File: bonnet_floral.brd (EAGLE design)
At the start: 65 x 30 mm, 10 parts, among them IC1 RASPBERRY_PI_ZERO_W_(V1.3)-WO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

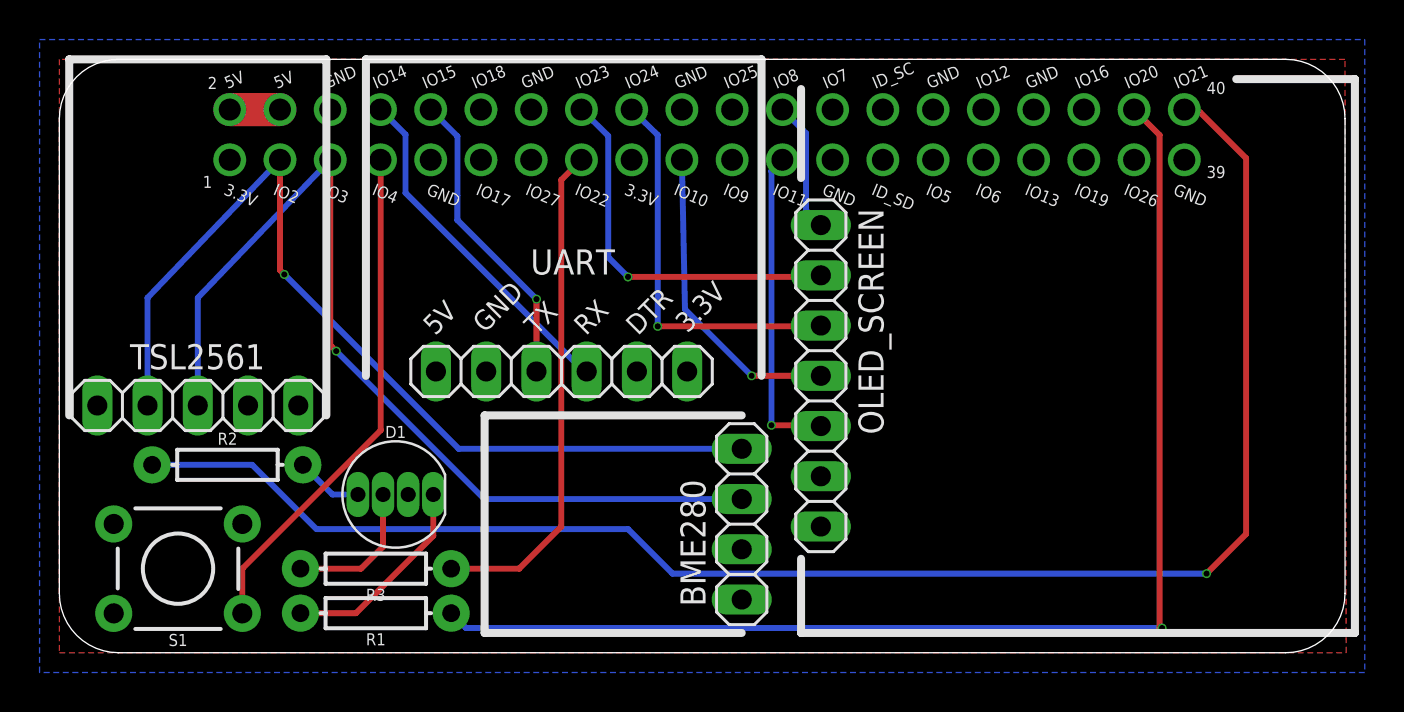
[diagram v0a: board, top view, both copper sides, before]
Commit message: Moving the BME280 down a little
The BME280 was right up against the lower side of the CP2102, so
I'm moving it down 1mm (and re-routing the signals as needed) to
give it a little bit of space.
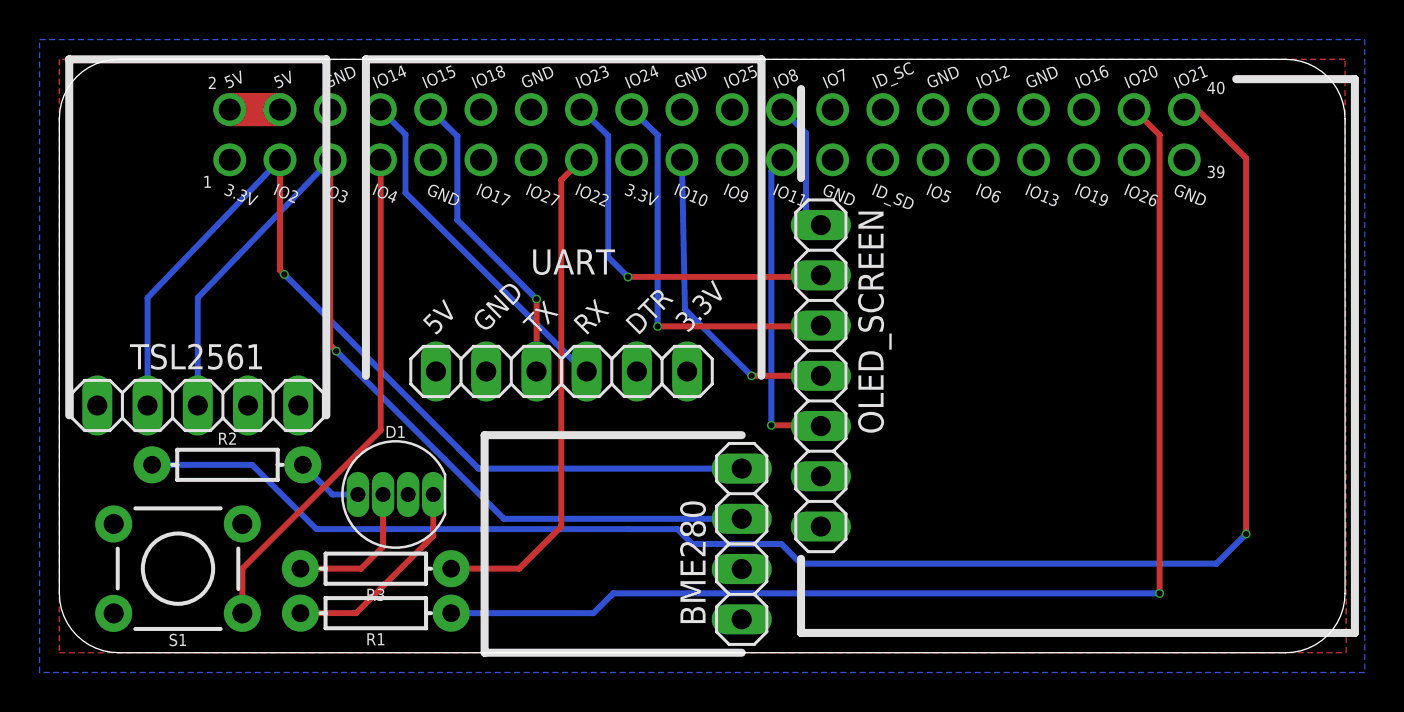
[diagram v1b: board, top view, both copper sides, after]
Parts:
- moved BME280 1.00 mm to (34.5, 5.50)
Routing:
- net RGB_R: track 63.1 -> 61.2 mm
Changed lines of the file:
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@@
 <setting verticaltext="up"/>
 </settings>
-<grid distance="1" unitdist="mm" unit="mm" style="lines" multiple="1" display="no" altdistance="0.125" altunitdist="mm" altunit="mm"/>
+<grid distance="1" unitdist="mm" unit="mm" style="lines" multiple="1" display="no" altdistance="0.5" altunitdist="mm" altunit="mm"/>
 <layers>
 <layer number="1" name="Top" color="4" fill="1" visible="yes" active="yes"/>
@@
 <wire x1="15.5" y1="30" x2="15.5" y2="14" width="0.4064" layer="21"/>
 <wire x1="35.5" y1="30" x2="15.5" y2="30" width="0.4064" layer="21"/>
-<wire x1="34.5" y1="1" x2="21.5" y2="1" width="0.4064" layer="21"/>
-<wire x1="21.5" y1="1" x2="21.5" y2="12" width="0.4064" layer="21"/>
-<wire x1="34.5" y1="12" x2="21.5" y2="12" width="0.4064" layer="21"/>
+<wire x1="34.5" y1="0" x2="21.5" y2="0" width="0.4064" layer="21"/>
+<wire x1="21.5" y1="0" x2="21.5" y2="11" width="0.4064" layer="21"/>
+<wire x1="34.5" y1="11" x2="21.5" y2="11" width="0.4064" layer="21"/>
 <wire x1="13.5" y1="12" x2="13.5" y2="30" width="0.4064" layer="21"/>
 <wire x1="0.5" y1="12" x2="0.5" y2="30" width="0.4064" layer="21"/>
@@
 <attribute name="VALUE" x="41.675" y="5.11" size="1.27" layer="27" rot="R90"/>
 </element>
-<element name="BME280" library="pinhead" package="1X04" value="" x="34.5" y="6.5" smashed="yes" rot="R270">
-<attribute name="NAME" x="32.6712" y="2.3438" size="1.27" layer="25" ratio="10" rot="R90"/>
-<attribute name="VALUE" x="31.325" y="11.58" size="1.27" layer="27" rot="R270"/>
+<element name="BME280" library="pinhead" package="1X04" value="" x="34.5" y="5.5" smashed="yes" rot="R270">
+<attribute name="NAME" x="32.6712" y="1.3438" size="1.27" layer="25" ratio="10" rot="R90"/>
+<attribute name="VALUE" x="31.325" y="10.58" size="1.27" layer="27" rot="R270"/>
 </element>
 <element name="D1" library="SparkFun-LED" package="LED-RGB-THRU@1" value="CLEAR" x="17" y="8">
@@
 <contactref element="IC1" pad="38-IO20"/>
 <contactref element="R1" pad="P$1"/>
-<wire x1="19.81" y1="2" x2="20.56" y2="1.25" width="0.3" layer="16"/>
-<wire x1="20.56" y1="1.25" x2="55.75" y2="1.25" width="0.3" layer="16"/>
-<via x="55.75" y="1.25" extent="1-16" drill="0.3048"/>
 <wire x1="54.335" y1="27.46" x2="55.625" y2="26.17" width="0.3" layer="1"/>
-<wire x1="55.625" y1="26.17" x2="55.625" y2="1.25" width="0.3" layer="1"/>
-<wire x1="55.625" y1="1.25" x2="55.75" y2="1.25" width="0.3" layer="1"/>
+<wire x1="55.625" y1="26.17" x2="55.625" y2="3" width="0.3" layer="1"/>
+<wire x1="19.81" y1="2" x2="27" y2="2" width="0.3048" layer="16"/>
+<wire x1="27" y1="2" x2="28" y2="3" width="0.3048" layer="16"/>
+<wire x1="28" y1="3" x2="55.625" y2="3" width="0.3048" layer="16"/>
+<via x="55.625" y="3" extent="1-16" drill="0.3048"/>
 </signal>
 <signal name="RGB_B">
 <contactref element="IC1" pad="40-IO21"/>
 <contactref element="R2" pad="P$1"/>
-<wire x1="28.75" y1="6.25" x2="31" y2="4" width="0.3" layer="16"/>
-<wire x1="31" y1="4" x2="58" y2="4" width="0.3" layer="16"/>
-<via x="58" y="4" extent="1-16" drill="0.3048"/>
-<wire x1="58" y1="4" x2="60" y2="6" width="0.3" layer="1"/>
 <wire x1="60" y1="6" x2="60" y2="25" width="0.3" layer="1"/>
 <wire x1="60" y1="25" x2="57.665" y2="27.335" width="0.3" layer="1"/>
@@
 <wire x1="13" y1="6.25" x2="9.75" y2="9.5" width="0.3" layer="16"/>
 <wire x1="9.75" y1="9.5" x2="4.69" y2="9.5" width="0.3" layer="16"/>
+<wire x1="28.75" y1="6.25" x2="31.25" y2="6.25" width="0.3048" layer="16"/>
+<wire x1="31.25" y1="6.25" x2="32" y2="5.5" width="0.3048" layer="16"/>
+<wire x1="32" y1="5.5" x2="36.5" y2="5.5" width="0.3048" layer="16"/>
+<wire x1="36.5" y1="5.5" x2="37.5" y2="4.5" width="0.3048" layer="16"/>
+<wire x1="37.5" y1="4.5" x2="58.5" y2="4.5" width="0.3048" layer="16"/>
+<wire x1="58.5" y1="4.5" x2="60" y2="6" width="0.3048" layer="16"/>
+<via x="60" y="6" extent="1-16" drill="0.3048"/>
 </signal>
 <signal name="UART_DTR">
@@
 <wire x1="13.695" y1="24.92" x2="7" y2="17.945" width="0.3" layer="16"/>
 <wire x1="7" y1="17.945" x2="7" y2="12.5" width="0.3" layer="16"/>
-<wire x1="34.5" y1="7.77" x2="21.48" y2="7.77" width="0.3" layer="16"/>
 <wire x1="21.48" y1="7.77" x2="14" y2="15.25" width="0.3" layer="16"/>
 <via x="14" y="15.25" extent="1-16" drill="0.3048"/>
 <wire x1="14" y1="15.25" x2="13.695" y2="15.555" width="0.3" layer="1"/>
 <wire x1="13.695" y1="15.555" x2="13.695" y2="24.92" width="0.3" layer="1"/>
+<wire x1="21.48" y1="7.77" x2="22.48" y2="6.77" width="0.3048" layer="16"/>
+<wire x1="22.48" y1="6.77" x2="34.5" y2="6.77" width="0.3048" layer="16"/>
 </signal>
 <signal name="I2C_SDA">
@@
 <wire x1="11.155" y1="24.92" x2="4.46" y2="17.945" width="0.3" layer="16"/>
 <wire x1="4.46" y1="17.945" x2="4.46" y2="12.5" width="0.3" layer="16"/>
-<wire x1="34.5" y1="10.31" x2="20.19" y2="10.31" width="0.3" layer="16"/>
 <wire x1="20.19" y1="10.31" x2="11.375" y2="19.125" width="0.3" layer="16"/>
 <wire x1="11.155" y1="24.92" x2="11.155" y2="19.345" width="0.3" layer="1"/>
 <wire x1="11.155" y1="19.345" x2="11.375" y2="19.125" width="0.3" layer="1"/>
 <via x="11.375" y="19.125" extent="1-16" drill="0.3048"/>
+<wire x1="20.19" y1="10.31" x2="21.19" y2="9.31" width="0.3048" layer="16"/>
+<wire x1="21.19" y1="9.31" x2="34.5" y2="9.31" width="0.3048" layer="16"/>
 </signal>
 <signal name="TSL_INT">

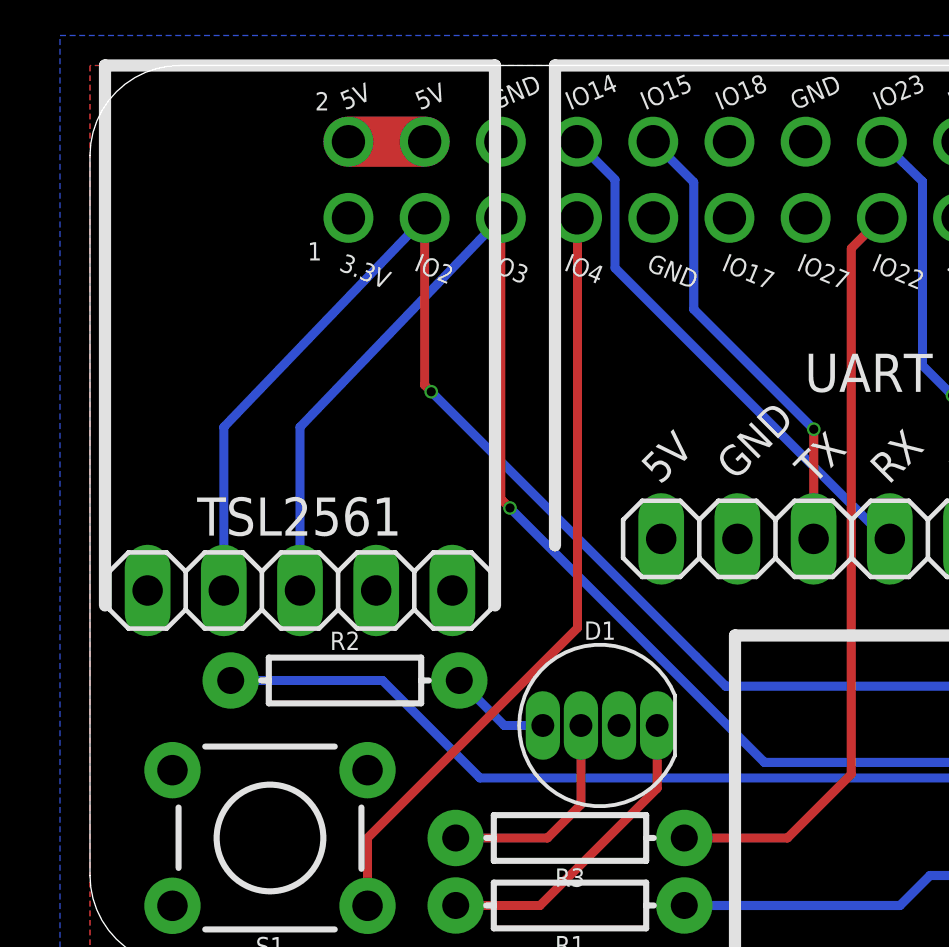
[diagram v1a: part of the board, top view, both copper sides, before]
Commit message: Adjusting the back silkscreen, adding artwork to board
Also cleaning up the DRC checks from before

removing https:// from the board url to make it bigger
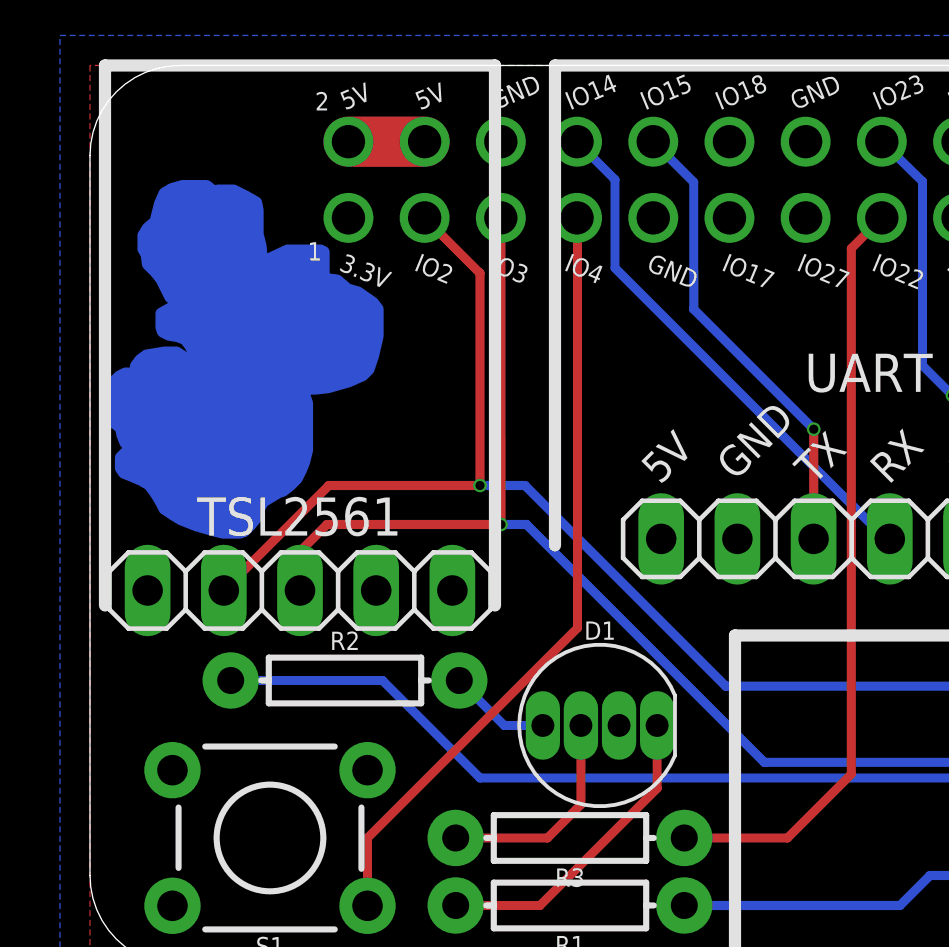
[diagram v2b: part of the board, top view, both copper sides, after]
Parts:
- added U$1: (no value), Artwork:FLORAL_SMALLER_MIRROR
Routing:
- net I2C_SCL: track 48.9 -> 42.7 mm
- net I2C_SDA: track 48.2 -> 43.9 mm
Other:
- board text added: "Floral Bonnet V0.9.1 John 'Warthog9' Hawley (C) 2018 CC-BY-SA 4.0"
- board text added: "github.com/unreproducible/bonnet_floral"
- board text removed: "Floral Bonnet V0.9.1 John 'Warthog9' Hawley (C) 2018 CC-BY-SA 4.0 https://github.com/unreproducible/bonnet_floral"
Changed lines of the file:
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@@
 <setting verticaltext="up"/>
 </settings>
-<grid distance="1" unitdist="mm" unit="mm" style="lines" multiple="1" display="no" altdistance="0.5" altunitdist="mm" altunit="mm"/>
+<grid distance="0.0025" unitdist="inch" unit="inch" style="lines" multiple="1" display="yes" altdistance="0.1" altunitdist="mm" altunit="mm"/>
 <layers>
 <layer number="1" name="Top" color="4" fill="1" visible="yes" active="yes"/>
@@
 <layer number="207" name="207bmp" color="8" fill="10" visible="yes" active="yes"/>
 <layer number="208" name="208bmp" color="9" fill="10" visible="yes" active="yes"/>
-<layer number="209" name="209bmp" color="7" fill="1" visible="yes" active="yes"/>
-<layer number="210" name="210bmp" color="7" fill="1" visible="yes" active="yes"/>
-<layer number="211" name="211bmp" color="7" fill="1" visible="yes" active="yes"/>
-<layer number="212" name="212bmp" color="7" fill="1" visible="yes" active="yes"/>
-<layer number="213" name="213bmp" color="7" fill="1" visible="yes" active="yes"/>
-<layer number="214" name="214bmp" color="7" fill="1" visible="yes" active="yes"/>
-<layer number="215" name="215bmp" color="7" fill="1" visible="yes" active="yes"/>
+<layer number="209" name="209bmp" color="10" fill="10" visible="yes" active="yes"/>
+<layer number="210" name="210bmp" color="11" fill="10" visible="yes" active="yes"/>
+<layer number="211" name="211bmp" color="12" fill="10" visible="yes" active="yes"/>
+<layer number="212" name="212bmp" color="13" fill="10" visible="yes" active="yes"/>
+<layer number="213" name="213bmp" color="14" fill="10" visible="yes" active="yes"/>
+<layer number="214" name="214bmp" color="15" fill="10" visible="yes" active="yes"/>
+<layer number="215" name="215bmp" color="16" fill="10" visible="yes" active="yes"/>
 <layer number="216" name="216bmp" color="7" fill="1" visible="yes" active="yes"/>
 <layer number="217" name="217bmp" color="18" fill="1" visible="no" active="no"/>
@@
 <wire x1="37.5" y1="1" x2="37.5" y2="4.75" width="0.4064" layer="21"/>
 <wire x1="37.5" y1="24" x2="37.5" y2="28.5" width="0.4064" layer="21"/>
-<text x="62" y="16" size="0.7" layer="22" rot="MR90" align="center">Floral Bonnet V0.9.1
+<text x="52.3415" y="7.5" size="1.143" layer="22" font="vector" rot="MR0" align="center">Floral Bonnet V0.9.1
 John 'Warthog9' Hawley
-(C) 2018 CC-BY-SA 4.0
-https://github.com/unreproducible/bonnet_floral</text>
-<text x="55" y="12" size="1.016" layer="22" rot="MR270" align="center">Specifically Designed for:
+(C) 2018 CC-BY-SA 4.0</text>
+<text x="52.3415" y="19.635" size="1.143" layer="22" font="vector" rot="MR180" align="center">Specifically Designed for:
 E-ALE https://e-ale.org/
 for linux.conf.au 2019</text>
@@
 <text x="29.25" y="16" size="1.016" layer="22" rot="MR45">DTR</text>
 <text x="31.75" y="16.125" size="1.016" layer="22" rot="MR45">3.3V</text>
+<text x="50.357" y="4" size="0.8636" layer="22" font="vector" rot="MR0" align="center">github.com/unreproducible/bonnet_floral</text>
 </plain>
 <attributes>
@@
 <attribute name="PROD_ID" value=" " x="16" y="4.25" size="1.778" layer="27" rot="R180" display="off"/>
 </element>
+<element name="U$1" library="Artwork" package="FLORAL_SMALLER_MIRROR" value="" x="5.134" y="20.2295" rot="MR0"/>
 </elements>
 <signals>
@@
 <contactref element="BME280" pad="2"/>
 <contactref element="IC1" pad="5-IO3"/>
-<wire x1="13.695" y1="24.92" x2="7" y2="17.945" width="0.3" layer="16"/>
-<wire x1="7" y1="17.945" x2="7" y2="12.5" width="0.3" layer="16"/>
-<wire x1="21.48" y1="7.77" x2="14" y2="15.25" width="0.3" layer="16"/>
-<via x="14" y="15.25" extent="1-16" drill="0.3048"/>
-<wire x1="14" y1="15.25" x2="13.695" y2="15.555" width="0.3" layer="1"/>
-<wire x1="13.695" y1="15.555" x2="13.695" y2="24.92" width="0.3" layer="1"/>
-<wire x1="21.48" y1="7.77" x2="22.48" y2="6.77" width="0.3048" layer="16"/>
 <wire x1="22.48" y1="6.77" x2="34.5" y2="6.77" width="0.3048" layer="16"/>
+<wire x1="13.695" y1="24.92" x2="13.7" y2="14.7" width="0.3048" layer="1"/>
+<via x="13.7" y="14.7" extent="1-16" drill="0.3048"/>
+<wire x1="7" y1="12.5" x2="7" y2="13.8" width="0.3048" layer="1"/>
+<wire x1="7" y1="13.8" x2="7.9" y2="14.7" width="0.3048" layer="1"/>
+<wire x1="7.9" y1="14.7" x2="13.7" y2="14.7" width="0.3048" layer="1"/>
+<wire x1="22.48" y1="6.77" x2="14.55" y2="14.7" width="0.3048" layer="16"/>
+<wire x1="14.55" y1="14.7" x2="13.7" y2="14.7" width="0.3048" layer="16"/>
 </signal>
 <signal name="I2C_SDA">
@@
 <contactref element="BME280" pad="1"/>
 <contactref element="IC1" pad="3-IO2"/>
-<wire x1="11.155" y1="24.92" x2="4.46" y2="17.945" width="0.3" layer="16"/>
-<wire x1="4.46" y1="17.945" x2="4.46" y2="12.5" width="0.3" layer="16"/>
-<wire x1="20.19" y1="10.31" x2="11.375" y2="19.125" width="0.3" layer="16"/>
-<wire x1="11.155" y1="24.92" x2="11.155" y2="19.345" width="0.3" layer="1"/>
-<wire x1="11.155" y1="19.345" x2="11.375" y2="19.125" width="0.3" layer="1"/>
-<via x="11.375" y="19.125" extent="1-16" drill="0.3048"/>
-<wire x1="20.19" y1="10.31" x2="21.19" y2="9.31" width="0.3048" layer="16"/>
 <wire x1="21.19" y1="9.31" x2="34.5" y2="9.31" width="0.3048" layer="16"/>
+<wire x1="11.155" y1="24.92" x2="13" y2="23.075" width="0.3048" layer="1"/>
+<wire x1="13" y1="23.075" x2="13" y2="16" width="0.3048" layer="1"/>
+<via x="13" y="16" extent="1-16" drill="0.3048"/>
+<wire x1="4.46" y1="12.5" x2="7.96" y2="16" width="0.3048" layer="1"/>
+<wire x1="7.96" y1="16" x2="13" y2="16" width="0.3048" layer="1"/>
+<wire x1="21.19" y1="9.31" x2="14.5" y2="16" width="0.3048" layer="16"/>
+<wire x1="14.5" y1="16" x2="13" y2="16" width="0.3048" layer="16"/>
 </signal>
 <signal name="TSL_INT">
@@
 <contactref element="UART" pad="1"/>
 </signal>
+<signal name="N$4">
+</signal>
 </signals>
